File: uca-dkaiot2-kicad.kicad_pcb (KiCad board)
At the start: 2 copper layers, 73 x 77.5 mm, 184 parts, among them J1 Conn_01x04, J10 Conn_Coaxial, J11 Conn_01x02, J12 Conn_01x02, J20 Conn_01x01, J21 Conn_01x01, J22 Conn_01x01, J23 Conn_01x01, J24 Conn_01x01, J25 Conn_01x01, J26 Conn_01x01, J2J14 Conn_02x06_Odd_Even, J3 Conn_01x02, J4 Conn_01x02, J5 Conn_01x02, J6 Conn_Coaxial, J7 Conn_01x05, J8 USB_B_Micro, J9J13 Conn_ARM_SWD_TagConnect_TC203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, U1 NCV8170AXV300T2G, U10 NCV8170AXV300T2G, U11 DRV5023AJxLPG, U12 R5478N101CD, U13 FDV301N, U14 FDV301N, U15 R5478N101CD, U16 FDV301N, U17 FDV301N, U18 LTR-303ALS-01, U19 ICM-20948, U2 Quectel_L96, U20 KXTJ3-1057, U21 HP203B, U22 SPH0645LM4H, U24 KX023-1025, U26 NCV8170BXV180T2G, U28 BSS138L, U29 SGP30, U3 Conn_01x04, U30 BSS138L, U31 BSS138L, U32 Micro_SD_Card_Det1, U33 NCV8170AXV300T2G, U4 STM32U595RITx, U5 E22-900M22S, U6 LSM303AH, U7 BME280, U8 ATECC608A-SSHDA, U9 MCP73831-2-OT, X1 SMD3225-4, X2 SMD2012-2

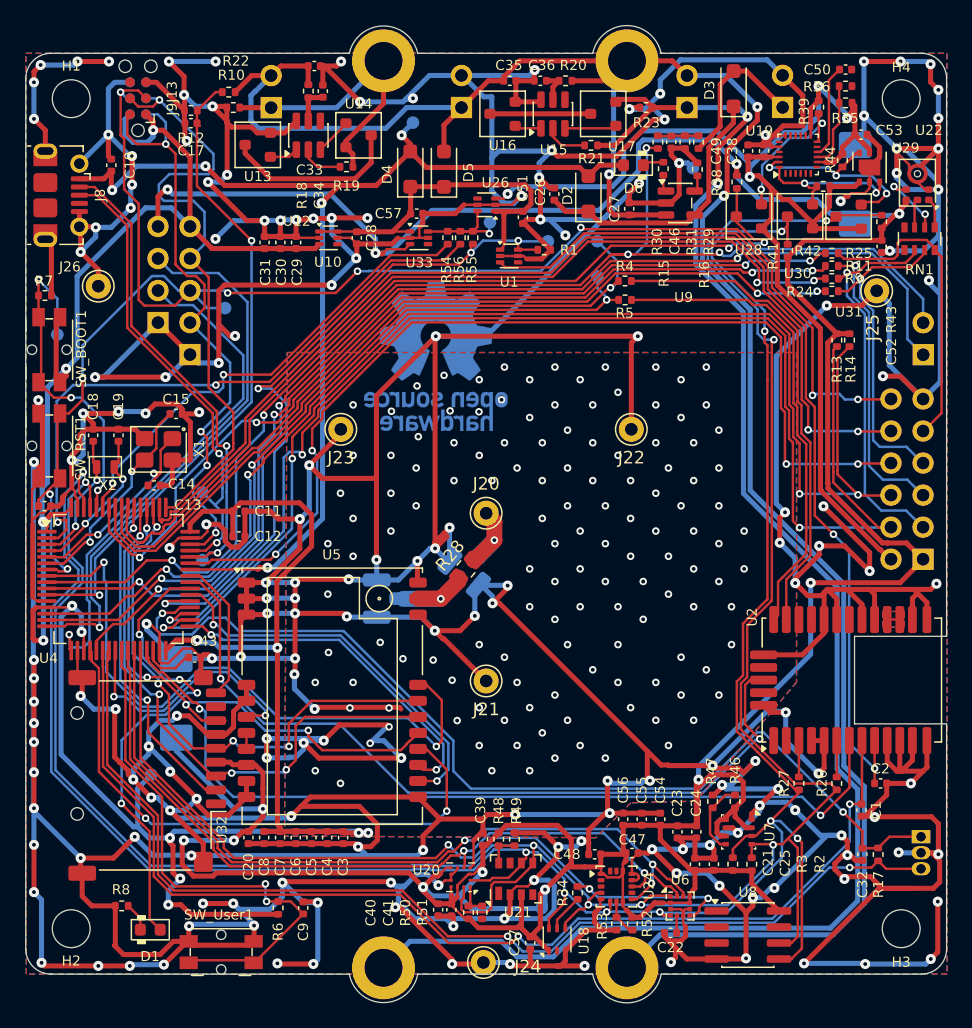
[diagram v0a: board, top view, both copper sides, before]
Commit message: WIP: remove unneeded parts from PCB, add SPA06 and FHTC3 to schematics
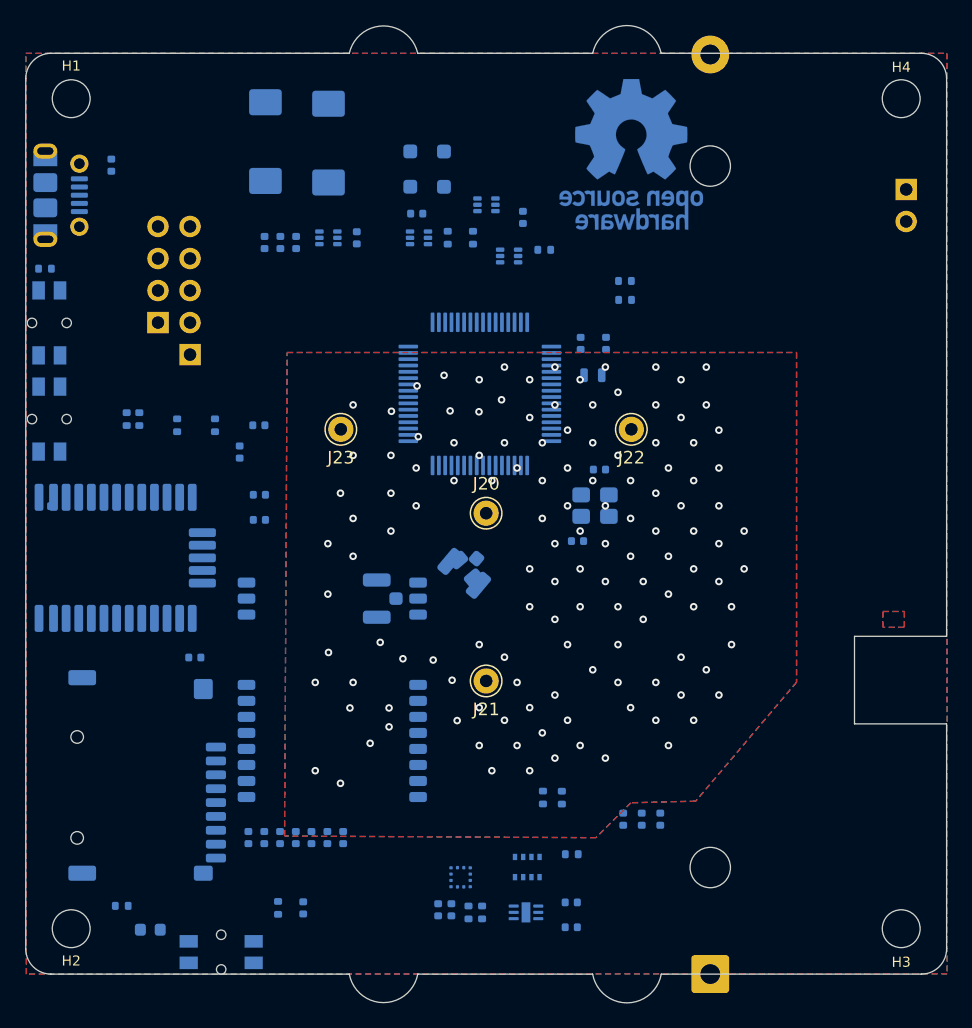
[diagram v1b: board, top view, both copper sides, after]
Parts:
- removed C17, C21, C23, C24, C25, C32, C33, C35, C38, C46, C47, C48, C49, C50, C52, C53: 100nF, Capacitor_SMD:C_0402_1005Metric
- removed C22: 220nF, Capacitor_SMD:C_0402_1005Metric
- removed C26, C27, C39: 4.7µF, Capacitor_SMD:C_0402_1005Metric
- removed C34, C36: 10nF, Capacitor_SMD:C_0402_1005Metric
- removed C37: 1µF, Capacitor_SMD:C_0402_1005Metric
- removed D2, D3: MBR120LSF, Diode_SMD:D_SOD-123F
- removed D6: XL-1608SURC-06, PCM_LED_SMD_AKL:LED_0603_1608Metric
- removed J11, J12, J3: Conn_01x02, Connector_PinHeader_2.54mm:PinHeader_1x02_P2.54mm_Vertical
- removed J24, J25, J26: Conn_01x01, Connector_Pin:Pin_D1.0mm_L10.0mm
- removed J2J14: Conn_02x06_Odd_Even, Connector_PinSocket_2.54mm:PinSocket_2x06_P2.54mm_Vertical
- removed J4: Conn_01x02, Connector_PinSocket_2.54mm:PinSocket_1x02_P2.54mm_Vertical
- removed J9J13: Conn_ARM_SWD_TagConnect_TC2030-NL, footprints:Tag-Connect_TC2030-IDC-NL_2x03_P1.27mm_Vertical_TopBottom
- removed J_3V1, J_5V1, J_BOOT1, J_D+1, J_D-1, J_GND1, J_GPS_EN1, J_PERIPH_3V1, J_PERIPH_CTRL1, J_RST1, J_RX1, J_TX1: TestPoint, TestPoint:TestPoint_Pad_D1.0mm
- removed R10, R31: 1M, Resistor_SMD:R_0402_1005Metric
- removed R11, R24, R25, R9: 51, Resistor_SMD:R_0402_1005Metric
- removed R12: 2M, Resistor_SMD:R_0402_1005Metric
- removed R15: 470, Resistor_SMD:R_0402_1005Metric
- removed R16: 2.5k, Resistor_SMD:R_0402_1005Metric
- removed R17, R38, R39: 4.7k, Resistor_SMD:R_0402_1005Metric
- removed R18, R20: 330, Resistor_SMD:R_0402_1005Metric
- removed R19, R21: 1k, Resistor_SMD:R_0402_1005Metric
- removed R22, R23, R30, R34, R35, R36, R46, R47, R48, R49, R52, R53, R56: 0, Resistor_SMD:R_0402_1005Metric
- removed R29: 4M, Resistor_SMD:R_0402_1005Metric
- removed R41, R42, R43, R44: 10k, Resistor_SMD:R_0402_1005Metric
- removed RN1: 0, Resistor_SMD:R_Array_Convex_4x0603
- removed U11: DRV5023AJxLPG, Package_TO_SOT_THT:TO-92_Inline
- removed U12, U15: R5478N101CD, Package_TO_SOT_SMD:SOT-23-6
- removed U13, U14, U16, U17: FDV301N, PCM_Package_TO_SOT_SMD_AKL:SOT-23
- removed U18: LTR-303ALS-01, OptoDevice:Lite-On_LTR-303ALS-01
- removed U19: ICM-20948, Sensor_Motion:InvenSense_QFN-24_3x3mm_P0.4mm
- removed U21: HP203B, footprints:LGA-8_3.6x3.8mm_P0.9mm
- removed U22: SPH0645LM4H, Sensor_Audio:Knowles_SPH0645LM4H-6_3.5x2.65mm
- removed U24: KX023-1025, Package_LGA:LGA-16_3x3mm_P0.5mm_LayoutBorder3x5y
- removed U28, U30, U31: BSS138L, PCM_Package_TO_SOT_SMD_AKL:SOT-23
- removed U29: SGP30, footprints:Sensirion_DFN-6-1EP_2.44x2.44mm_P0.8mm
- removed U3: Conn_01x04, footprints:BAT-TH_BH-18650-A1BJ034
- removed U6: LSM303AH, Package_LGA:LGA-12_2x2mm_P0.5mm
- removed U7: BME280, Package_LGA:Bosch_LGA-8_2.5x2.5mm_P0.65mm_ClockwisePinNumbering
- removed U8: ATECC608A-SSHDA, Package_SO:SOIC-8_3.9x4.9mm_P1.27mm
- removed U9: MCP73831-2-OT, Package_TO_SOT_SMD:SOT-23-5
- added BT1: Battery_Cell, Battery:BatteryHolder_MPD_BK-18650-PC2, B.Cu at (79.3, 95.0)
- added C58: 100nF, Capacitor_SMD:C_0402_1005Metric, B.Cu at (68.2, 89.3)
- added C59: 100nF, Capacitor_SMD:C_0402_1005Metric, B.Cu at (68.2, 91.3)
- added R57: 0, Resistor_SMD:R_0402_1005Metric, B.Cu at (68.3, 85.5)
- added U23: SPA06-003, Package_LGA:Bosch_LGA-8_2x2.5mm_P0.65mm_ClockwisePinNumbering, B.Cu at (64.8, 86.5)
- added U25: FHTC3, Package_DFN_QFN:DFN-6-1EP_2x2mm_P0.5mm_EP0.7x1.6mm, B.Cu at (64.7, 90.1)
- C1, C10, C11, C12, C13, C14, C15, C18, C19, C2, C20, C28, C29, C3, C30, C31, C4, C40, C41, C43, C5, C51, C54, C55, C56, C57, C6, C7, C8, C9, D1, D4, D5, J8, R1, R13, R14, R2, R26, R27, R28, R3, R4, R5, R50, R51, R54, R55, R6, R7, R8, SW_BOOT1, SW_RST1, SW_User1, U1, U10, U2, U20, U26, U32, U33, U4, U5, X1, X2: moved to B.Cu
- moved U2 59.3 mm to (32.0, 62.0)
- moved C1 56.9 mm to (42.0, 53.6)
- moved R26 56.9 mm to (40.0, 51.5)
- moved R27 56.9 mm to (37.0, 51.5)
- moved C2 56.9 mm to (43.5, 51.5), turned to 180 degrees
- moved R13 56.6 mm to (33.0, 51.0)
- moved R14 56.6 mm to (34.0, 51.0)
- moved C16 46.9 mm to (44.0, 29.0)
- moved C42 45.6 mm to (49.0, 29.1)
- moved C19 39.3 mm to (71.0, 45.0)
- moved C18 39.3 mm to (69.0, 45.0)
- moved X2 39.3 mm to (70.0, 47.5), turned to 0 degrees
- moved C14 35.3 mm to (70.5, 55.0)
- moved X1 34.9 mm to (70.1, 57.9)
- moved C15 33.4 mm to (68.7, 60.7)
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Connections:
- net I2C3_SCL renamed I2C2_SCL
- net I2C3_SDA renamed I2C2_SDA
- R54 pad 2: V_PERIPH_CTRL -> SD_ON_OFF
- R55 pad 2: V_PERIPH_CTRL -> SD_ON_OFF
- U26 pad 6: V_PERIPH_CTRL -> SD_ON_OFF
- U33 pad 6: V_PERIPH_CTRL -> SD_ON_OFF
- U4 pad 55: Net-(U4-PB3) -> SAI_SCK
- U4 pad 56: Net-(U4-PB4) -> SAI_MCLK
- U4 pad 57: Net-(U4-PB5) -> SAI_SD
- U4 pad 58: Net-(U4-PB6) -> SAI_FS
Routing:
- net GND: track 1371.6 -> 0.00 mm, vias 319 -> 131
- net V_PERIPH_3V: track 316.6 -> 0.00 mm, vias 12 -> 0
- net +3V: track 205.4 -> 0.00 mm, vias 13 -> 0
- net I2C1_SCL: track 197.6 -> 0.00 mm, vias 7 -> 0
- net I2C1_SDA: track 189.0 -> 0.00 mm, vias 9 -> 0
- net +BATT1_IN: track 174.4 -> 0.00 mm, vias 3 -> 0
- net MCU_RESET: track 130.9 -> 0.00 mm, vias 9 -> 0
- net -BATT2_IN: track 126.7 -> 0.00 mm, vias 2 -> 0
- net +5V: track 116.4 -> 0.00 mm, vias 5 -> 0
- net VDD_1V8: track 108.5 -> 0.00 mm, vias 4 -> 0
- net I2C2_SDA: track 106.0 -> 0.00 mm, vias 3 -> 0
- net PC2_ADC: track 102.9 -> 0.00 mm, vias 5 -> 0
- net I2C2_SCL: track 100.6 -> 0.00 mm, vias 4 -> 0
- net PA5_DAC_ADC: track 90.1 -> 0.00 mm, vias 3 -> 0
- net V_BCKP_On_Off: track 89.8 -> 0.00 mm, vias 2 -> 0
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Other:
- board text removed: "+"
- board text removed: "BATTERY"
- board text removed: "SOLAR"
- board text removed: "−"

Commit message: WIP: BOM
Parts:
- removed C16, C42: 470µF, Capacitor_Tantalum_SMD:CP_EIA-7343-15_Kemet-W
- removed C31, C56: 10nF, Capacitor_SMD:C_0402_1005Metric
- removed C40, C41: 100nF, Capacitor_SMD:C_0402_1005Metric
- removed D4, D5: MBR120LSF, Diode_SMD:D_SOD-123F
- removed J6: Conn_Coaxial, Connector_Coaxial:U.FL_Hirose_U.FL-R-SMT-1_Vertical
- removed R28: 0, Resistor_SMD:R_0805_2012Metric
- removed R50, R51: 0, Resistor_SMD:R_0402_1005Metric
- removed U20: KXTJ3-1057, Package_LGA:Kionix_LGA-12_2x2mm_P0.5mm_LayoutBorder2x4y
- added C101: 4.7µF, Capacitor_SMD:C_0402_1005Metric, F.Cu at (26.9, 103.9)
- added C104: 100uF/6.3V, Capacitor_SMD:C_1206_3216Metric, F.Cu at (25.0, 91.9)
- added C105: 4.7µF, Capacitor_SMD:C_0402_1005Metric, F.Cu at (26.9, 102.0)
- added C106: 2.2uF, Capacitor_SMD:C_0402_1005Metric, F.Cu at (26.9, 100.0)
- added C107: 100nF, Capacitor_SMD:C_0402_1005Metric, F.Cu at (26.9, 98.0)
- added C108: 2.2uF, Capacitor_SMD:C_0402_1005Metric, F.Cu at (24.0, 105.9)
- added C109: 2.2uF, Capacitor_SMD:C_0402_1005Metric, F.Cu at (24.0, 103.9)
- added C111: 100nF, Capacitor_SMD:C_0402_1005Metric, F.Cu at (24.0, 100.0)
- added C112: 100nF/25V, Capacitor_SMD:C_0402_1005Metric, F.Cu at (169.3, 93.2)
- added C113: 100nF/25V, Capacitor_SMD:C_0402_1005Metric, F.Cu at (166.3, 91.1)
- added C114: 100nF/25V, Capacitor_SMD:C_0402_1005Metric, F.Cu at (187.9, 105.3)
- added C115: 100nF, Capacitor_SMD:C_0402_1005Metric, F.Cu at (33.0, 4.61)
- added C116: 4.7µF, Capacitor_SMD:C_0402_1005Metric, F.Cu at (110.9, 11.0)
- added C117: 820µF, Capacitor_SMD:CP_Elec_6.3x9.9, F.Cu at (116.2, 24.2)
- added C118: 2.2pF, Capacitor_SMD:C_0402_1005Metric, F.Cu at (86.7, 14.1)
- added C119: ~, Capacitor_SMD:C_0402_1005Metric, F.Cu at (86.7, 16.1)
- added C44: 22µF/25V, Capacitor_SMD:C_0805_2012Metric, F.Cu at (155.1, 131.1)
- added C45: 22µF/25V, Capacitor_SMD:C_0805_2012Metric, F.Cu at (155.1, 128.1)
- added C60: 22µF/25V, Capacitor_SMD:C_0805_2012Metric, F.Cu at (155.1, 125.1)
- added C61: 22µF/25V, Capacitor_SMD:C_0805_2012Metric, F.Cu at (155.1, 122.1)
- added C62: 4.7µF, Capacitor_SMD:C_0402_1005Metric, F.Cu at (86.9, 51.7)
- added C63: 100nF, Capacitor_SMD:C_0402_1005Metric, F.Cu at (86.9, 49.7)
- added C64: 100nF/25V, Capacitor_SMD:C_0402_1005Metric, F.Cu at (162.2, 122.5)
- added C65: 100nF/25V, Capacitor_SMD:C_0402_1005Metric, F.Cu at (176.2, 108.8)
- added C66: 220nF/10V, Capacitor_SMD:C_0402_1005Metric, F.Cu at (178.1, 104.4)
- added C68: 47µF/10V, Capacitor_SMD:C_1206_3216Metric, F.Cu at (145.2, 105.9)
- added C69: 4.7µF/10V, Capacitor_SMD:C_0805_2012Metric, F.Cu at (144.7, 109.2)
- added C70: 100nF, Capacitor_SMD:C_0402_1005Metric, F.Cu at (142.4, 109.2)
- added C71: 100nF, Capacitor_SMD:C_0402_1005Metric, F.Cu at (43.8, 18.7)
- added C72: 1uF, Capacitor_SMD:C_0402_1005Metric, F.Cu at (43.8, 16.7)
- added C73: 1uF, Capacitor_SMD:C_0402_1005Metric, F.Cu at (43.8, 14.7)
- added C74: 1uF, Capacitor_SMD:C_0402_1005Metric, F.Cu at (43.8, 12.8)
- added C75: 100nF, Capacitor_SMD:C_0402_1005Metric, F.Cu at (43.8, 10.8)
- added C76: 100nF, Capacitor_SMD:C_0402_1005Metric, F.Cu at (40.9, 18.7)
- added C77: 1uF/6.3V, Capacitor_SMD:C_0402_1005Metric, F.Cu at (40.9, 16.7)
- added C78: 1uF, Capacitor_SMD:C_0402_1005Metric, F.Cu at (40.9, 14.7)
- added C79: 4.7µF, Capacitor_SMD:C_0402_1005Metric, F.Cu at (40.9, 12.8)
- added C80: 100nF, Capacitor_SMD:C_0402_1005Metric, F.Cu at (40.9, 10.8)
- added C81: 1uF, Capacitor_SMD:C_0402_1005Metric, F.Cu at (38.0, 18.7)
- added C82: 4.7uF/6.3V, Capacitor_SMD:C_0402_1005Metric, F.Cu at (38.0, 16.7)
- added C83: 100uF/6.3V, Capacitor_SMD:C_1206_3216Metric, F.Cu at (58.2, 31.5)
- added C84: 100uF/6.3V, Capacitor_SMD:C_1206_3216Metric, F.Cu at (58.2, 28.2)
- added C85: 100uF/6.3V, Capacitor_SMD:C_1206_3216Metric, F.Cu at (58.2, 24.8)
- added C86: 100uF/6.3V, Capacitor_SMD:C_1206_3216Metric, F.Cu at (58.2, 21.5)
- added C87: 100uF/6.3V, Capacitor_SMD:C_1206_3216Metric, F.Cu at (58.2, 18.1)
- added C88: 100uF/6.3V, Capacitor_SMD:C_1206_3216Metric, F.Cu at (58.2, 14.8)
- added C89: 100uF/6.3V, Capacitor_SMD:C_1206_3216Metric, F.Cu at (58.2, 11.4)
- added C90: 100uF/6.3V, Capacitor_SMD:C_1206_3216Metric, F.Cu at (58.2, 8.07)
- added C91: 4.7µF, Capacitor_SMD:C_0402_1005Metric, F.Cu at (38.0, 14.7)
- added C92: 47µF/10V, Capacitor_SMD:C_1206_3216Metric, F.Cu at (25.0, 95.3)
- added C93: 100nF, Capacitor_SMD:C_0402_1005Metric, F.Cu at (29.7, 105.9)
- added C94: 4.7µF/10V, Capacitor_SMD:C_0805_2012Metric, F.Cu at (27.6, 87.9)
- added C95: 10nF, Capacitor_SMD:C_0402_1005Metric, F.Cu at (29.7, 103.9)
- added C96: 4.7µF, Capacitor_SMD:C_0402_1005Metric, F.Cu at (29.7, 102.0)
- added C97: 10nF, Capacitor_SMD:C_0402_1005Metric, F.Cu at (29.7, 100.0)
- added C98: 10nF, Capacitor_SMD:C_0402_1005Metric, F.Cu at (29.7, 98.0)
- added C99: 100nF, Capacitor_SMD:C_0402_1005Metric, F.Cu at (26.9, 105.9)
- added D10: PMEG6030ELPX, Diode_SMD:D_SOD-128, F.Cu at (147.9, 106.9)
- added D11: 1N5819WS, Diode_SMD:D_SOD-323, F.Cu at (27.7, 84.9)
- added D12: PMEG6030ELPX, Diode_SMD:D_SOD-128, F.Cu at (150.6, 45.7)
- added D7: KT-0603R, LED_SMD:LED_0603_1608Metric, F.Cu at (176.8, 107.1)
- added D8: KT-0603W, LED_SMD:LED_0603_1608Metric, F.Cu at (176.8, 105.7)
- added D9: PMEG6030ELPX, Diode_SMD:D_SOD-128, F.Cu at (160.2, 106.8)
- added F1: 3A, 81°C, Connector_Wire:SolderWire-0.127sqmm_1x02_P3.7mm_D0.48mm_OD1mm, F.Cu at (140.1, 108.8)
- added FB1: ~, Inductor_SMD:L_0603_1608Metric, F.Cu at (49.0, 6.46)
- added J19: Conn_01x02, Connector_JST:JST_XH_B2B-XH-A_1x02_P2.50mm_Vertical, F.Cu at (158.8, 40.3)
- added J27: Conn_01x02, Connector_JST:JST_XH_B2B-XH-A_1x02_P2.50mm_Vertical, F.Cu at (167.2, 40.3)
- added JP6: Jumper_2_Bridged, Jumper:SolderJumper-2_P1.3mm_Bridged2Bar_Pad1.0x1.5mm, F.Cu at (53.2, 17.9)
- added JP7: Jumper_2_Bridged, Jumper:SolderJumper-2_P1.3mm_Bridged2Bar_Pad1.0x1.5mm, F.Cu at (53.2, 14.3)
- added JP8: Jumper_2_Bridged, Jumper:SolderJumper-2_P1.3mm_Bridged2Bar_Pad1.0x1.5mm, F.Cu at (53.2, 10.8)
- added JP9: Jumper_2_Bridged, Jumper:SolderJumper-2_P1.3mm_Bridged2Bar_Pad1.0x1.5mm, F.Cu at (53.2, 7.22)
- added L1: 33µH/2.32A, Inductor_SMD:L_Chilisin_BMRB00060650, F.Cu at (154.0, 107.2)
- added Q1: AO3401A, Package_TO_SOT_SMD:SOT-23, F.Cu at (163.8, 108.7)
- added Q2: AO3401A, Package_TO_SOT_SMD:SOT-23, F.Cu at (163.8, 105.2)
- added Q3: AO3400A, Package_TO_SOT_SMD:SOT-23, F.Cu at (195.6, 105.2)
- added Q4: AO3400A, Package_TO_SOT_SMD:SOT-23, F.Cu at (195.6, 108.6)
- added Q5: AO3400A, Package_TO_SOT_SMD:SOT-23, F.Cu at (184.7, 108.6)
- added Q6: AO3400A, Package_TO_SOT_SMD:SOT-23, F.Cu at (184.7, 105.2)
- added R100: 4.7k, Resistor_SMD:R_0402_1005Metric, F.Cu at (32.6, 101.9)
- added R101: 0, Resistor_SMD:R_0402_1005Metric, F.Cu at (32.6, 99.9)
- added R102: 9.09k, Resistor_SMD:R_0603_1608Metric, F.Cu at (165.8, 79.5)
- added R103: 5.90k, Resistor_SMD:R_0603_1608Metric, F.Cu at (167.4, 79.5)
- added R104: 38.3k, Resistor_SMD:R_0603_1608Metric, F.Cu at (169.0, 79.5)
- added R105: 21.5k, Resistor_SMD:R_0603_1608Metric, F.Cu at (170.6, 79.5)
- added R106: 100, Resistor_SMD:R_0402_1005Metric, F.Cu at (187.9, 104.3)
- added R107: 0.1, Resistor_SMD:R_1206_3216Metric, F.Cu at (191.1, 108.8)
- added R108: 2k, Resistor_SMD:R_0402_1005Metric, F.Cu at (187.9, 106.4)
- added R111: 2k, Resistor_SMD:R_0402_1005Metric, F.Cu at (181.7, 107.7)
- added R112: 2k, Resistor_SMD:R_0402_1005Metric, F.Cu at (181.7, 104.2)
- added R114: 4.7k, Resistor_SMD:R_0402_1005Metric, F.Cu at (105.2, 24.6)
- added R32: 0.150, Resistor_SMD:R_1206_3216Metric, F.Cu at (161.7, 131.6)
- added R33: 0.150, Resistor_SMD:R_1206_3216Metric, F.Cu at (161.7, 128.3)
- added R37: 33k, Resistor_SMD:R_0402_1005Metric, F.Cu at (170.8, 111.1)
- added R40: 12k, Resistor_SMD:R_0402_1005Metric, F.Cu at (170.9, 118.7)
- added R45: 10k, Resistor_SMD:R_0402_1005Metric, F.Cu at (179.2, 105.7)
- added R58: 10k, Resistor_SMD:R_0402_1005Metric, F.Cu at (179.2, 107.2)
- added R60: 120, Resistor_SMD:R_0402_1005Metric, F.Cu at (176.2, 104.4)
- added R63: 47k, Resistor_SMD:R_0402_1005Metric, F.Cu at (91.3, 57.0)
- added R65: 47k, Resistor_SMD:R_0402_1005Metric, F.Cu at (91.3, 55.0)
- added R70: 0.150, Resistor_SMD:R_1206_3216Metric, F.Cu at (142.9, 105.9)
- added R74: 4.7k, Resistor_SMD:R_0402_1005Metric, F.Cu at (49.6, 18.7)
- added R75: 2.2k, Resistor_SMD:R_0402_1005Metric, F.Cu at (49.6, 16.7)
- added R77: 2.2k, Resistor_SMD:R_0402_1005Metric, F.Cu at (49.6, 14.7)
- added R78: 0, Resistor_SMD:R_0402_1005Metric, F.Cu at (49.6, 12.7)
- added R79: 0, Resistor_SMD:R_0402_1005Metric, F.Cu at (49.6, 10.7)
- added R80: 0, Resistor_SMD:R_0402_1005Metric, F.Cu at (49.6, 8.71)
- added R81: 47k, Resistor_SMD:R_0402_1005Metric, F.Cu at (46.7, 18.7)
- added R82: 47k, Resistor_SMD:R_0402_1005Metric, F.Cu at (46.7, 16.7)
- added R83: 47k, Resistor_SMD:R_0402_1005Metric, F.Cu at (46.7, 14.7)
- added R84: 47k, Resistor_SMD:R_0402_1005Metric, F.Cu at (46.7, 12.7)
- added R85: 0, Resistor_SMD:R_0402_1005Metric, F.Cu at (30.1, 14.3)
- added R86: 0, Resistor_SMD:R_0402_1005Metric, F.Cu at (30.1, 12.3)
- added R87: 10, Resistor_SMD:R_0402_1005Metric, F.Cu at (46.7, 10.7)
- added R88: 2.2k, Resistor_SMD:R_0402_1005Metric, F.Cu at (38.4, 105.9)
- added R89: 11k, Resistor_SMD:R_0402_1005Metric, F.Cu at (38.4, 103.9)
- added R90: 23k, Resistor_SMD:R_0402_1005Metric, F.Cu at (38.4, 101.9)
- added R91: 10k, Resistor_SMD:R_0402_1005Metric, F.Cu at (38.4, 99.9)
- added R92: 2.2k, Resistor_SMD:R_0402_1005Metric, F.Cu at (38.4, 97.9)
- added R93: 4.7k, Resistor_SMD:R_0402_1005Metric, F.Cu at (35.5, 105.9)
- added R94: 100k, Resistor_SMD:R_0402_1005Metric, F.Cu at (35.5, 103.9)
- added R95: 0, Resistor_SMD:R_0402_1005Metric, F.Cu at (35.5, 101.9)
- added R96: 100k, Resistor_SMD:R_0402_1005Metric, F.Cu at (35.5, 99.9)
- added R97: 4.7k, Resistor_SMD:R_0402_1005Metric, F.Cu at (35.5, 97.9)
- added R98: 10k, Resistor_SMD:R_0402_1005Metric, F.Cu at (32.6, 105.9)
- added R99: 100k, Resistor_SMD:R_0402_1005Metric, F.Cu at (32.6, 103.9)
- added RV1: 200k, Potentiometer_SMD:Potentiometer_Bourns_3314J_Vertical, F.Cu at (170.9, 114.8)
- added RV3: 200k, Potentiometer_SMD:Potentiometer_Bourns_3314J_Vertical, F.Cu at (36.9, 93.2)
- added RV4: 200k, Potentiometer_SMD:Potentiometer_Bourns_3314J_Vertical, F.Cu at (30.8, 93.2)
- added SW1: SW_Reed, Resistor_THT:R_Axial_DIN0207_L6.3mm_D2.5mm_P10.16mm_Horizontal, F.Cu at (152.1, 4.40)
- added TP1: TestPoint, TestPoint_Pad_D0.5mm:TestPoint_Pad_D0.5mm, F.Cu at (38.0, 8.89)
- added TP2: TestPoint, TestPoint_Pad_D0.5mm:TestPoint_Pad_D0.5mm, F.Cu at (38.0, 7.07)
- added TP3: TestPoint, TestPoint_Pad_D0.5mm:TestPoint_Pad_D0.5mm, F.Cu at (38.0, 5.25)
- added U27: INA3221, Package_DFN_QFN:Texas_RGV0016A_VQFN-16-1EP_4x4mm_P0.65mm_EP2.1x2.1mm, F.Cu at (87.0, 55.8)
- added U34: CN3801, CN3791:SSOP-10_L4.9-W3.9-P1.00-LS6.0-BL, F.Cu at (170.6, 106.8)
- added U35: TLV320ADC3101, QFN_drill0.3:VQFN-24-1EP_4x4mm_P0.5mm_EP2.5x2.5mm_ThermalVias_drill0.3, F.Cu at (158.1, 51.4)
- added U36: ISL21080CIH315Z-TK, Package_TO_SOT_SMD:SOT-23, F.Cu at (32.3, 87.2)
- added U37: RT9080-30GJ5, Package_TO_SOT_SMD:TSOT-23-5, F.Cu at (37.3, 87.0)
- added U38: OPA379AIDCK, Package_TO_SOT_SMD:SOT-353_SC-70-5, F.Cu at (41.9, 105.1)
- added U41: TLV7031DCK, Package_TO_SOT_SMD:SOT-353_SC-70-5, F.Cu at (41.9, 94.5)
- added U42: H2112-CB, Package_TO_SOT_SMD:SOT-23-6, F.Cu at (191.4, 105.2)
- added U43: TMP390, Package_TO_SOT_SMD:SOT-563, F.Cu at (169.3, 91.7)
- added U44: TMP390, Package_TO_SOT_SMD:SOT-563, F.Cu at (166.4, 92.7)
- added U45: LSM6DS3TR-C, Package_LGA:LGA-14_3x2.5mm_P0.5mm_LayoutBorder3x4y, F.Cu at (29.0, 17.4)
- added U46: RT9080-30GJ5, Package_TO_SOT_SMD:TSOT-23-5, F.Cu at (123.5, 17.9)
- added U47: RT9080-18GJ5, Package_TO_SOT_SMD:TSOT-23-5, F.Cu at (123.5, 13.3)
- BT1: footprint Battery:BatteryHolder_MPD_BK-18650-PC2 -> 18650:BatteryHolder_18650-Ambient; moved to F.Cu
- C1, C10, C11, C12, C13, C14, C15, C2, C20, C28, C29, C3, C30, C4, C43, C5, C51, C54, C55, C57, C58, C59, C6, C7, C8, C9, J10, R1, R13, R14, R2, R26, R27, R3, R4, R5, R54, R55, R6, R7, SW_BOOT1, SW_RST1, SW_User1, SYM1, U2, U23, U25, U32, U4, U5, X1: moved to F.Cu
- C18, C19: value 5.6pF -> 12pF; moved to F.Cu
- D1: value LED_0603_Blue -> LED_0805_Green; footprint PCM_LED_SMD_AKL:LED_0603_1608Metric -> PCM_LED_SMD_AKL:LED_0805_2012Metric; moved to F.Cu
- J1: footprint Connector_PinHeader_2.54mm:PinHeader_1x04_P2.54mm_Vertical -> Connector_JST:JST_XH_B4B-XH-A_1x04_P2.50mm_Vertical; moved to F.Cu
- J20, J21, J22, J23: moved to B.Cu
- J5: footprint Connector_PinHeader_2.54mm:PinHeader_1x02_P2.54mm_Vertical -> Connector_JST:JST_XH_B2B-XH-A_1x02_P2.50mm_Vertical; moved to F.Cu
- J7: footprint Connector_PinHeader_2.54mm:PinHeader_1x05_P2.54mm_Vertical -> Connector_JST:JST_XH_B5B-XH-A_1x05_P2.50mm_Vertical; moved to F.Cu
- J8: footprint Connector_USB:USB_Micro-B_Molex-105017-0001 -> Connector_USB:USB_Micro-B_Amphenol_10118194-0001LF_Horizontal; moved to F.Cu
- R57: value 0 -> 47k; moved to F.Cu
- R8: value 360 -> 1k; moved to F.Cu
- U1, U10, U33: value NCV8170AXV300T2G -> RT9080-30GJ5; footprint Package_TO_SOT_SMD:SOT-563 -> Package_TO_SOT_SMD:TSOT-23-5; moved to F.Cu
- U26: value NCV8170BXV180T2G -> OPA2391DGKR; footprint Package_TO_SOT_SMD:SOT-563 -> PCM_Package_SO_AKL:MSOP-8_3x3mm_P0.65mm; moved to F.Cu
- X2: value SMD2012-2 -> SMD3215-2 32.768kHz; footprint PCM_Crystal_AKL:Crystal_SMD_2012-2Pin_2.0x1.2mm -> PCM_Crystal_AKL:Crystal_SMD_3215-2Pin_3.2x1.5mm; moved to F.Cu
- moved H1 190.6 mm to (201.0, 106.8), turned to 180 degrees
- moved H2 179.6 mm to (201.0, 41.0), turned to 180 degrees
- moved U32 165.3 mm to (197.8, 53.5), turned to -90 degrees
- moved SW_User1 160.8 mm to (192.0, 39.3)
- moved SW_BOOT1 157.5 mm to (184.3, 39.4), turned to 0 degrees
- moved SW_RST1 150.1 mm to (176.5, 39.4), turned to 0 degrees
- moved J23 132.8 mm to (179.6, 80.6)
- moved U5 132.0 mm to (180.6, 59.4)
- moved J8 115.4 mm to (143.0, 41.0), turned to 180 degrees
- moved J20 107.7 mm to (168.1, 73.9)
- moved J21 107.2 mm to (168.1, 60.6)
- moved U2 106.7 mm to (138.7, 60.7), turned to -90 degrees
- moved X2 100.8 mm to (168.4, 69.1), turned to -90 degrees
- moved U4 99.0 mm to (158.4, 66.9)
- moved H4 90.9 mm to (135.2, 106.8), turned to 180 degrees
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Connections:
- BT1 pad 1: unconnected-(BT1-+-Pad1) -> +BATT_UNPROT
- BT1 pad 2: unconnected-(BT1---Pad2) -> -BATT_UNPROT
- C1 pad 2: GND -> -BATT_PROT
- C10 pad 2: GND -> -BATT_PROT
- C11 pad 2: GND -> -BATT_PROT
- C12 pad 2: GND -> -BATT_PROT
- C13 pad 2: GND -> -BATT_PROT
- C14 pad 2: GND -> -BATT_PROT
- C15 pad 2: GND -> -BATT_PROT
- C18 pad 2: GND -> -BATT_PROT
- C19 pad 2: GND -> -BATT_PROT
- C2 pad 1: Net-(U1-OUT) -> Net-(U1-VOUT)
- C2 pad 2: GND -> -BATT_PROT
- C20 pad 1: V_PERIPH_3V -> +3V0_PERIPH
- C20 pad 2: GND -> -BATT_PROT
- C28 pad 1: Vin -> +BATT_PROT
- C28 pad 2: GND -> -BATT_PROT
- C29 pad 2: GND -> -BATT_PROT
- C3 pad 2: GND -> -BATT_PROT
- C30 pad 2: GND -> -BATT_PROT
- C4 pad 2: GND -> -BATT_PROT
- C43 pad 2: GND -> -BATT_PROT
- C5 pad 2: GND -> -BATT_PROT
- C51 pad 1: Vin -> +BATT_PROT
- C51 pad 2: GND -> -BATT_PROT
- C54 pad 1: V_PERIPH_3V -> +3V0_PERIPH
- C54 pad 2: GND -> -BATT_PROT
- C55 pad 1: V_PERIPH_3V -> +3V0_PERIPH
- C55 pad 2: GND -> -BATT_PROT
- C57 pad 1: Vin -> +BATT_PROT
- C57 pad 2: GND -> -BATT_PROT
- C58 pad 1: V_PERIPH_3V -> +3V0_PERIPH
- C58 pad 2: GND -> -BATT_PROT
- C59 pad 1: V_PERIPH_3V -> +3V0_PERIPH
- C59 pad 2: GND -> -BATT_PROT
- C6 pad 2: GND -> -BATT_PROT
- C7 pad 2: GND -> -BATT_PROT
- C8 pad 2: GND -> -BATT_PROT
- C9 pad 2: GND -> -BATT_PROT
- J1 pad 1: GND -> -BATT_PROT
- J1 pad 4: V_PERIPH_3V -> +3V0_PERIPH
- J10 pad 2: GND -> -BATT_PROT
- J21 pad 1: GND -> -BATT_PROT
- J22 pad 1: GND -> -BATT_PROT
- J23 pad 1: GND -> -BATT_PROT
- J5 pad 1: SOLAR -> CSIP
- J5 pad 2: GND -> -BATT_PROT
- J7 pad 1: GND -> -BATT_PROT
- J8 pad 5: GND -> -BATT_PROT
- J8 pad SH: GND -> -BATT_PROT
- R1 pad 2: GND -> -BATT_PROT
- R13 pad 1: V_PERIPH_3V -> +3V0_PERIPH
- R14 pad 1: V_PERIPH_3V -> +3V0_PERIPH
- R2 pad 2: V_PERIPH_3V -> +3V0_PERIPH
- R3 pad 2: V_PERIPH_3V -> +3V0_PERIPH
- R54 pad 1: V_PERIPH_ON_OFF -> V_PERIPH_CTRL
- R54 pad 2: SD_ON_OFF -> V_PERIPH_CTRL
- R55 pad 2: SD_ON_OFF -> V_PERIPH_CTRL
- R57 pad 2: GND -> -BATT_PROT
- R7 pad 2: GND -> -BATT_PROT
- R8 pad 2: GND -> -BATT_PROT
- SW_RST1 pad 1: GND -> -BATT_PROT
- SW_User1 pad 2: GND -> -BATT_PROT
- SYM1 pad 1: GND -> -BATT_PROT
- U1 pad 1: Vin -> +BATT_PROT
- U1 pad 2: GND -> -BATT_PROT
- U1 pad 3: Net-(U1-OUT) -> GPS_On_Off
- U1 pad 5: GND -> Net-(U1-VOUT)
- U10 pad 1: Vin -> +BATT_PROT
- U10 pad 2: GND -> -BATT_PROT
- U10 pad 3: +3V -> +BATT_PROT
- U10 pad 5: GND -> +3V
- U2 pad 10: GND -> -BATT_PROT
- U2 pad 11: GND -> -BATT_PROT
- U2 pad 12: GND -> -BATT_PROT
- U2 pad 13: GND -> -BATT_PROT
- U2 pad 14: GND -> -BATT_PROT
- U2 pad 15: GND -> -BATT_PROT
- U2 pad 18: GND -> -BATT_PROT
- U2 pad 19: GND -> -BATT_PROT
- U2 pad 21: GND -> -BATT_PROT
- U2 pad 22: GND -> -BATT_PROT
- U2 pad 27: GND -> -BATT_PROT
- U2 pad 31: GND -> -BATT_PROT
- U2 pad 4: GND -> -BATT_PROT
- U2 pad 5: GND -> -BATT_PROT
- U2 pad 9: Net-(U1-OUT) -> Net-(U1-VOUT)
- U23 pad 1: GND -> -BATT_PROT
- U23 pad 6: V_PERIPH_3V -> +3V0_PERIPH
- U23 pad 7: GND -> -BATT_PROT
- U23 pad 8: V_PERIPH_3V -> +3V0_PERIPH
- U25 pad 1: V_PERIPH_3V -> +3V0_PERIPH
- U25 pad 6: GND -> -BATT_PROT
- U25 pad 7: GND -> -BATT_PROT
- U26 pad 1: Vin -> Net-(U26B-+)
- U26 pad 2: GND -> Net-(U26A--)
- U26 pad 3: VDD_1V8 -> Net-(U26A-+)
- U26 pad 4: unconnected-(U26-NC-Pad4) -> GNDA
- U26 pad 5: GND -> Net-(U26B-+)
- U26 pad 6: SD_ON_OFF -> Net-(U26B--)
- U32 pad 4: V_PERIPH_3V -> +3V0_SD
- U32 pad 6: GND -> -BATT_PROT
- U32 pad SH: GND -> -BATT_PROT
- U33 pad 1: Vin -> +BATT_PROT
- U33 pad 2: GND -> -BATT_PROT
- U33 pad 3: V_PERIPH_3V -> V_PERIPH_CTRL
- U33 pad 5: GND -> +3V0_PERIPH
- U4 pad 12: GND -> -BATT_PROT
- U4 pad 18: GND -> -BATT_PROT
- U4 pad 2: SD_ON_OFF -> V_PERIPH_CTRL
- U4 pad 31: GND -> -BATT_PROT
- U4 pad 47: GND -> -BATT_PROT
- U4 pad 59: V_PERIPH_ON_OFF -> SD_ON_OFF
- U4 pad 63: GND -> -BATT_PROT
- U5 pad 1: GND -> -BATT_PROT
- U5 pad 10: GND -> -BATT_PROT
- U5 pad 11: GND -> -BATT_PROT
- U5 pad 12: GND -> -BATT_PROT
- U5 pad 2: GND -> -BATT_PROT
- U5 pad 20: GND -> -BATT_PROT
- U5 pad 22: GND -> -BATT_PROT
- U5 pad 3: GND -> -BATT_PROT
- U5 pad 4: GND -> -BATT_PROT
- U5 pad 5: GND -> -BATT_PROT
- U5 pad 9: V_PERIPH_3V -> +3V0_PERIPH
- X1 pad 2: GND -> -BATT_PROT
- X1 pad 4: GND -> -BATT_PROT
- X2 pad 1: Net-(U4-PC15) -> Net-(U4-PC14)
- X2 pad 2: Net-(U4-PC14) -> Net-(U4-PC15)
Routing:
- net GND: vias 131 -> 0
- added copper zone on B.Cu, net -BATT_PROT
- added copper zone on F.Cu, net -BATT_PROT
- added copper zone on In1.Cu, net -BATT_PROT
- added copper zone on In2.Cu, net -BATT_PROT
- removed copper zone on B.Cu, net GND
- removed copper zone on F.Cu, net GND
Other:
- outline, holes or cut-outs redrawn
- copper layers 2 -> 4
- board text removed: "3V"
- board text removed: "3V_PERIPH"
- board text removed: "BOOT"
- board text removed: "GND"
- board text removed: "I2C2_SCL"
- board text removed: "I2C2_SDA"
- board text removed: "IO1"
- board text removed: "IO2"
- board text removed: "MCU_RESET"
- board text removed: "PA2_TX"
- board text removed: "PA3_RX"
- board text removed: "PA5"
- board text removed: "PC2"
- board text removed: "RESET"
- board text removed: "SAI_FS"
- board text removed: "SAI_MCLK"
- board text removed: "SAI_SCK"
- board text removed: "SAI_SD"
- board text removed: "SWCLK"
- board text removed: "SWDIO"
- board text removed: "UCA DKAIoT2 KiCad v0.2 //piernov"
- board text removed: "UserButton"
- board text removed: "VDD_1V8"
- board text removed: "V_PERIPH_3V"

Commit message: WIP: omit some components and perform initial rough placement on PCB
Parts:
- removed C105, C91: 4.7µF, Capacitor_SMD:C_0402_1005Metric
- removed C73: 1uF, Capacitor_SMD:C_0402_1005Metric
- removed C77: 1uF/6.3V, Capacitor_SMD:C_0402_1005Metric
- removed C82: 4.7uF/6.3V, Capacitor_SMD:C_0402_1005Metric
- removed C83, C84, C85, C86, C87, C88, C89, C90: 100uF/6.3V, Capacitor_SMD:C_1206_3216Metric
- removed C92: 47µF/10V, Capacitor_SMD:C_1206_3216Metric
- removed FB1: ~, Inductor_SMD:L_0603_1608Metric
- removed J10: Conn_Coaxial, Connector_Coaxial:U.FL_Hirose_U.FL-R-SMT-1_Vertical
- removed JP6, JP7, JP8, JP9: Jumper_2_Bridged, Jumper:SolderJumper-2_P1.3mm_Bridged2Bar_Pad1.0x1.5mm
- removed R54, R55: 0, Resistor_SMD:R_0402_1005Metric
- removed R75: 2.2k, Resistor_SMD:R_0402_1005Metric
- removed R81, R83: 47k, Resistor_SMD:R_0402_1005Metric
- removed R87: 10, Resistor_SMD:R_0402_1005Metric
- removed TP1, TP2, TP3: TestPoint, TestPoint_Pad_D0.5mm:TestPoint_Pad_D0.5mm
- added C110: 4.7µF, Capacitor_SMD:C_0402_1005Metric, F.Cu at (159.3, 78.2)
- added C120: 4.7µF, Capacitor_SMD:C_0402_1005Metric, F.Cu at (152.4, 46.5)
- added C121: 47µF/10V, Capacitor_SMD:C_1206_3216Metric, F.Cu at (161.1, 79.9)
- added J6: Conn_Coaxial, Connector_Coaxial:U.FL_Hirose_U.FL-R-SMT-1_Vertical, F.Cu at (169.5, 69.5)
- added R28: 0, Resistor_SMD:R_0402_1005Metric, F.Cu at (171.7, 67.2)
- C104: value 100uF/6.3V -> 47uF/6.3V
- SYM1: moved to B.Cu
- moved R57 183.5 mm to (202.7, 78.5), turned to 90 degrees
- moved U23 180.4 mm to (200.6, 78.4), turned to 0 degrees
- moved U25 176.8 mm to (195.9, 78.6)
- moved C59 176.8 mm to (198.5, 78.5), turned to 90 degrees
- moved C58 174.4 mm to (195.9, 80.5)
- moved U45 173.7 mm to (191.5, 78.6), turned to 0 degrees
- moved C115 173.0 mm to (189.1, 79.2), turned to 90 degrees
- moved R86 171.7 mm to (189.1, 77.2), turned to -90 degrees
- moved R85 170.3 mm to (188.0, 78.3), turned to 90 degrees
- moved U26 157.8 mm to (168.2, 49.5)
- moved C99 155.8 mm to (170.6, 45.8), turned to 0 degrees
- moved C107 153.7 mm to (172.4, 48.5), turned to 0 degrees
- moved C109 153.0 mm to (168.2, 52.8), turned to 0 degrees
- moved C95 152.1 mm to (169.8, 44.8)
- moved C111 149.2 mm to (165.4, 52.3), turned to -90 degrees
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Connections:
- C101 pad 2: GNDA -> -BATT_PROT
- C104 pad 2: GNDA -> -BATT_PROT
- C106 pad 1: GNDA -> -BATT_PROT
- C107 pad 2: GNDA -> -BATT_PROT
- C108 pad 1: GNDA -> -BATT_PROT
- C109 pad 1: GNDA -> -BATT_PROT
- C111 pad 2: GNDA -> -BATT_PROT
- C118 pad 1: E22_ANT -> Net-(J6-In)
- C75 pad 1: +3.3VA -> +3VSBA
- C75 pad 2: GNDA -> -BATT_PROT
- C78 pad 1: +3.3VA -> +3VSBA
- C78 pad 2: GNDA -> -BATT_PROT
- C93 pad 2: GNDA -> -BATT_PROT
- C96 pad 2: GNDA -> -BATT_PROT
- C98 pad 2: GNDA -> -BATT_PROT
- C99 pad 2: GNDA -> -BATT_PROT
- J19 pad 2: GNDA -> -BATT_PROT
- J27 pad 2: GNDA -> -BATT_PROT
- R96 pad 2: GNDA -> -BATT_PROT
- R99 pad 2: GNDA -> -BATT_PROT
- U26 pad 4: GNDA -> -BATT_PROT
- U35 pad 10: +3.3VA -> +3VSBA
- U35 pad 25: GNDA -> -BATT_PROT
- U35 pad 9: GNDA -> -BATT_PROT
- U36 pad 3: GNDA -> -BATT_PROT
- U38 pad 2: GNDA -> -BATT_PROT
- U41 pad 2: GNDA -> -BATT_PROT
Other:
- board size 73 x 77.5 mm -> 73 x 73 mm
